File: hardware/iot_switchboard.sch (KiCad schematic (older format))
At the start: 15 parts, among them IC1 ATTINY84-M, P1 CONN_01X05, P2 CONN_01X05, T1 CONN_01X01

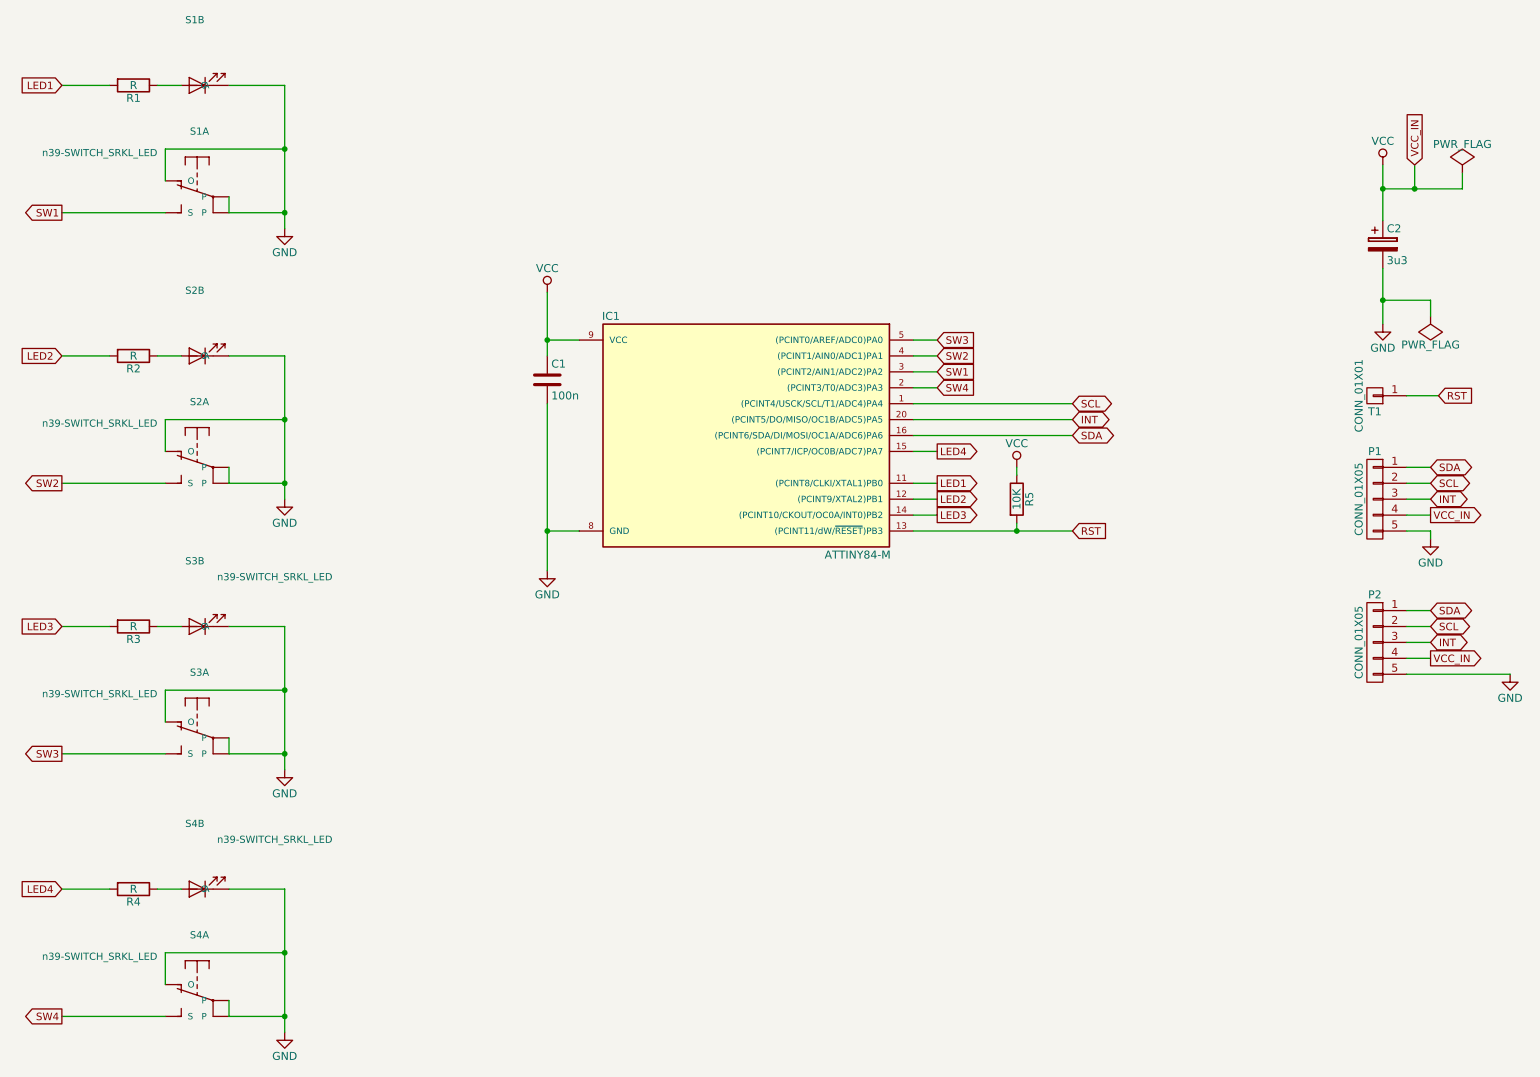
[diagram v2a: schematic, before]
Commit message: Reduce to 2 switches and adapt outline
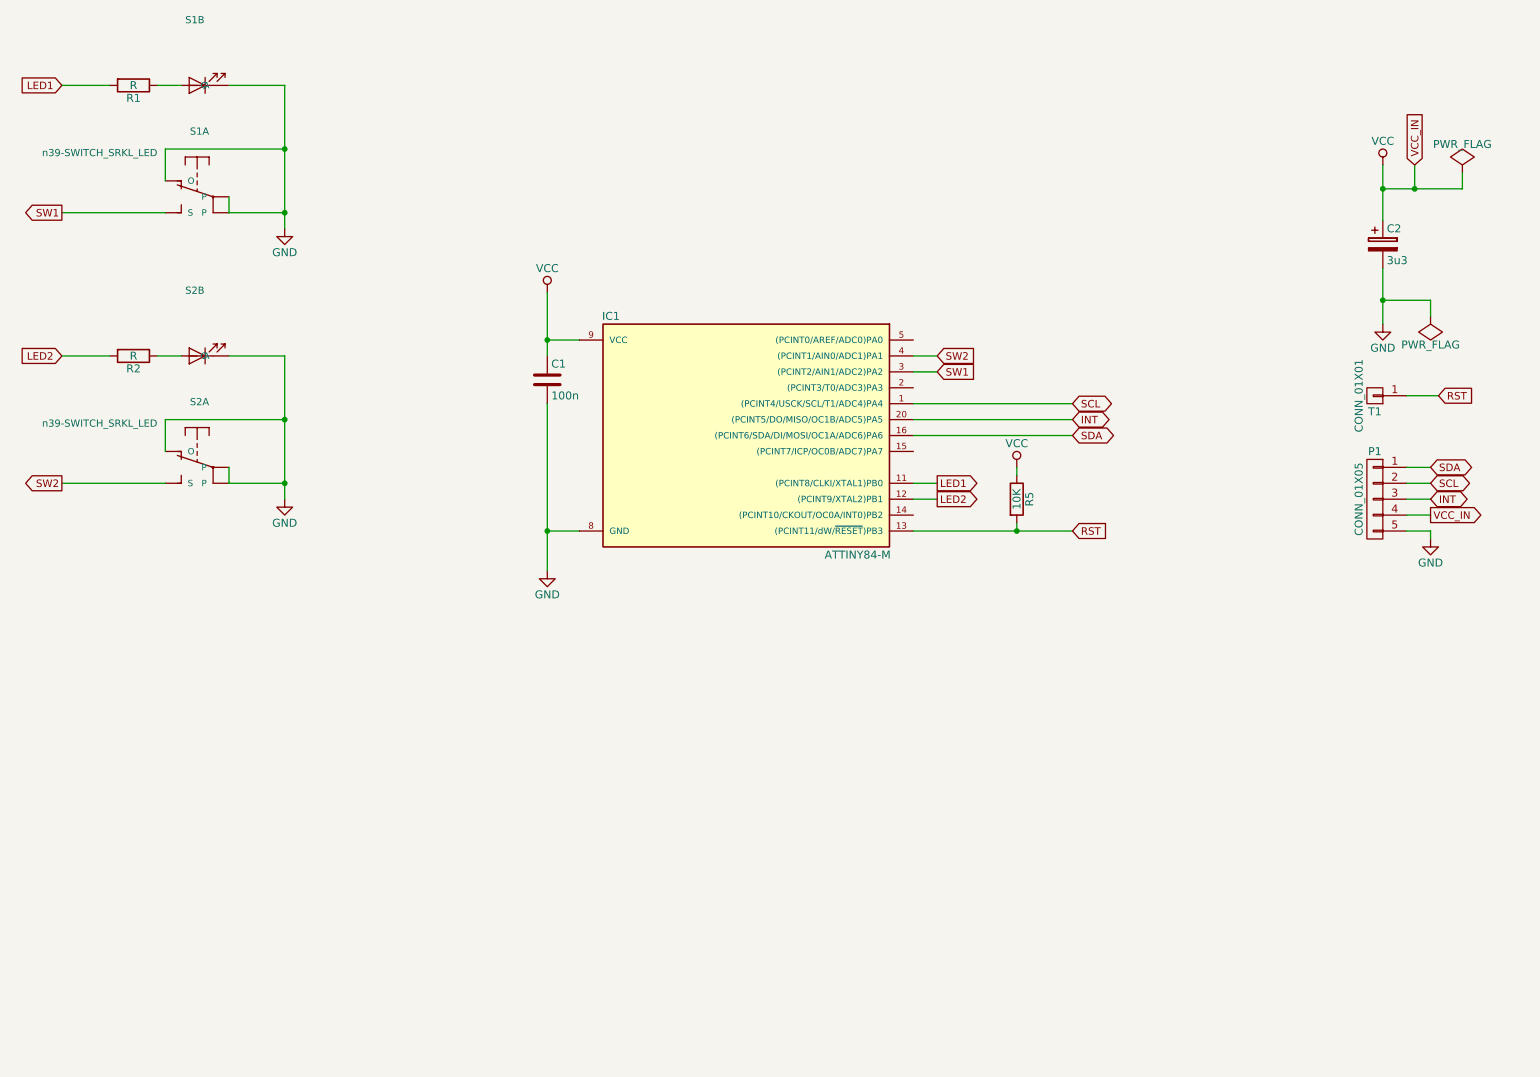
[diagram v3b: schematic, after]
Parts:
- removed P2: CONN_01X05, Socket_Strips:Socket_Strip_Straight_1x05, symbol CONN_01X05
- removed R3, R4: R, Resistors_Universal:Resistor_SMD+THTuniversal_0805to1206_RM10_HandSoldering, symbol R
- removed S3, S4: n39-SWITCH_SRKL_LED, n39-SWITCH_SRKL_LED, symbol n39-SWITCH_SRKL_LED
- P1: footprint Socket_Strips:Socket_Strip_Straight_1x05 -> Pin_Headers:Pin_Header_Straight_1x05
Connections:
- net LED3: no longer names the net of IC1.14 ((PCINT10/CKOUT/OC0A/INT0)PB2)
- net LED4: no longer names the net of IC1.15 ((PCINT7/ICP/OC0B/ADC7)PA7)
- net SW3: no longer names the net of IC1.5 ((PCINT0/AREF/ADC0)PA0)
- net SW4: no longer names the net of IC1.2 ((PCINT3/T0/ADC3)PA3)
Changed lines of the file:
@@
-$EndComp
-$Comp
-L n39-SWITCH_SRKL_LED S3
-U 1 1 58C873ED
-P 1900 5350
-F 0 "S3" V 1515 5275 45  0000 L BNN
-F 1 "n39-SWITCH_SRKL_LED" V 1650 5600 45  0000 L BNN
-F 2 "n39-SWITCH_SRKL_LED" H 1930 5500 20  0001 C CNN
-F 3 "" H 1900 5350 60  0001 C CNN
-	1    1900 5350
-	0    -1   1    0
-$EndComp
-$Comp
-L n39-SWITCH_SRKL_LED S3
-U 2 1 58C873F4
-P 1900 4650
-F 0 "S3" V 1515 4575 45  0000 L BNN
-F 1 "n39-SWITCH_SRKL_LED" V 1615 4775 45  0000 L BNN
-F 2 "n39-SWITCH_SRKL_LED" H 1930 4800 20  0001 C CNN
-F 3 "" H 1900 4650 60  0001 C CNN
-	2    1900 4650
-	0    1    1    0
-$EndComp
-$Comp
-L R R3
-U 1 1 58C873FB
-P 1500 4650
-F 0 "R3" V 1580 4650 50  0000 C CNN
-F 1 "R" V 1500 4650 50  0000 C CNN
-F 2 "Resistors_Universal:Resistor_SMD+THTuniversal_0805to1206_RM10_HandSoldering" V 1430 4650 50  0001 C CNN
-F 3 "" H 1500 4650 50  0000 C CNN
-	1    1500 4650
-	0    1    1    0
 $EndComp
 $Comp
 L GND #PWR03
-U 1 1 58C87402
-P 2450 5550
-F 0 "#PWR03" H 2450 5300 50  0001 C CNN
-F 1 "GND" H 2450 5400 50  0000 C CNN
-F 2 "" H 2450 5550 50  0000 C CNN
-F 3 "" H 2450 5550 50  0000 C CNN
-	1    2450 5550
-	1    0    0    -1
-$EndComp
-$Comp
-L n39-SWITCH_SRKL_LED S4
-U 1 1 58C87589
-P 1900 7000
-F 0 "S4" V 1515 6925 45  0000 L BNN
-F 1 "n39-SWITCH_SRKL_LED" V 1650 7250 45  0000 L BNN
-F 2 "n39-SWITCH_SRKL_LED" H 1930 7150 20  0001 C CNN
-F 3 "" H 1900 7000 60  0001 C CNN
-	1    1900 7000
-	0    -1   1    0
-$EndComp
-$Comp
-L n39-SWITCH_SRKL_LED S4
-U 2 1 58C87590
-P 1900 6300
-F 0 "S4" V 1515 6225 45  0000 L BNN
-F 1 "n39-SWITCH_SRKL_LED" V 1615 6425 45  0000 L BNN
-F 2 "n39-SWITCH_SRKL_LED" H 1930 6450 20  0001 C CNN
-F 3 "" H 1900 6300 60  0001 C CNN
-	2    1900 6300
-	0    1    1    0
-$EndComp
-$Comp
-L R R4
-U 1 1 58C87597
-P 1500 6300
-F 0 "R4" V 1580 6300 50  0000 C CNN
-F 1 "R" V 1500 6300 50  0000 C CNN
-F 2 "Resistors_Universal:Resistor_SMD+THTuniversal_0805to1206_RM10_HandSoldering" V 1430 6300 50  0001 C CNN
-F 3 "" H 1500 6300 50  0000 C CNN
-	1    1500 6300
-	0    1    1    0
-$EndComp
-$Comp
-L GND #PWR04
-U 1 1 58C8759E
-P 2450 7200
-F 0 "#PWR04" H 2450 6950 50  0001 C CNN
-F 1 "GND" H 2450 7050 50  0000 C CNN
-F 2 "" H 2450 7200 50  0000 C CNN
-F 3 "" H 2450 7200 50  0000 C CNN
-	1    2450 7200
-	1    0    0    -1
-$EndComp
-$Comp
-L GND #PWR05
 U 1 1 58C8805A
 P 4100 4300
-F 0 "#PWR05" H 4100 4050 50  0001 C CNN
+F 0 "#PWR03" H 4100 4050 50  0001 C CNN
 F 1 "GND" H 4100 4150 50  0000 C CNN
 F 2 "" H 4100 4300 50  0000 C CNN
@@
 $EndComp
 $Comp
-L VCC #PWR06
+L VCC #PWR04
 U 1 1 58C880BC
 P 4100 2550
-F 0 "#PWR06" H 4100 2400 50  0001 C CNN
+F 0 "#PWR04" H 4100 2400 50  0001 C CNN
 F 1 "VCC" H 4100 2700 50  0000 C CNN
 F 2 "" H 4100 2550 50  0000 C CNN
@@
 	1350 2950 1050 2950
 Wire Wire Line
-	2450 5450 2100 5450
-Wire Wire Line
-	2450 4650 2450 5550
-Wire Wire Line
-	2100 4650 2450 4650
-Connection ~ 2450 5450
-Wire Wire Line
-	1650 4650 1800 4650
-Wire Wire Line
-	1350 4650 1050 4650
-Wire Wire Line
-	2450 7100 2100 7100
-Wire Wire Line
-	2450 6300 2450 7200
-Wire Wire Line
-	2100 6300 2450 6300
-Connection ~ 2450 7100
-Wire Wire Line
-	1650 6300 1800 6300
-Wire Wire Line
-	1350 6300 1050 6300
-Wire Wire Line
 	4100 2550 4100 2950
 Wire Wire Line
@@
 $EndComp
 $Comp
-L VCC #PWR07
+L VCC #PWR05
 U 1 1 58C8935E
 P 7050 3650
-F 0 "#PWR07" H 7050 3500 50  0001 C CNN
+F 0 "#PWR05" H 7050 3500 50  0001 C CNN
 F 1 "VCC" H 7050 3800 50  0000 C CNN
 F 2 "" H 7050 3650 50  0000 C CNN
@@
 Text GLabel 1050 2950 0    47   Input ~ 0
 LED2
-Text GLabel 1050 4650 0    47   Input ~ 0
-LED3
-Text GLabel 1050 6300 0    47   Input ~ 0
-LED4
 Text GLabel 6550 3750 2    47   Output ~ 0
 LED1
 Text GLabel 6550 3850 2    47   Output ~ 0
 LED2
-Text GLabel 6550 3950 2    47   Output ~ 0
-LED3
-Text GLabel 6550 3550 2    47   Output ~ 0
-LED4
 Text GLabel 6550 3050 2    47   Input ~ 0
 SW1
 Text GLabel 6550 2950 2    47   Input ~ 0
 SW2
-Text GLabel 6550 2850 2    47   Input ~ 0
-SW3
-Text GLabel 6550 3150 2    47   Input ~ 0
-SW4
 Text GLabel 1050 2050 0    47   Output ~ 0
 SW1
 Text GLabel 1050 3750 0    47   Output ~ 0
 SW2
-Text GLabel 1050 5450 0    47   Output ~ 0
-SW3
-Text GLabel 1050 7100 0    47   Output ~ 0
-SW4
 Text GLabel 7400 4050 2    47   Input ~ 0
 RST
@@
 SDA
 $Comp
-L VCC #PWR08
+L VCC #PWR06
 U 1 1 58C8C38E
 P 9350 1750
-F 0 "#PWR08" H 9350 1600 50  0001 C CNN
+F 0 "#PWR06" H 9350 1600 50  0001 C CNN
 F 1 "VCC" H 9350 1900 50  0000 C CNN
 F 2 "" H 9350 1750 50  0000 C CNN
@@
 $EndComp
 $Comp
-L GND #PWR09
+L GND #PWR07
 U 1 1 58C8C3DE
 P 9350 2750
-F 0 "#PWR09" H 9350 2500 50  0001 C CNN
+F 0 "#PWR07" H 9350 2500 50  0001 C CNN
 F 1 "GND" H 9350 2600 50  0000 C CNN
 F 2 "" H 9350 2750 50  0000 C CNN
@@
 F 0 "P1" H 9300 4150 50  0000 C CNN
 F 1 "CONN_01X05" V 9400 3850 50  0000 C CNN
-F 2 "Socket_Strips:Socket_Strip_Straight_1x05" H 9300 3850 50  0001 C CNN
+F 2 "Pin_Headers:Pin_Header_Straight_1x05" H 9300 3850 50  0001 C CNN
 F 3 "" H 9300 3850 50  0000 C CNN
 	1    9300 3850
@@
 INT
 $Comp
-L GND #PWR010
+L GND #PWR08
 U 1 1 58C8F67F
 P 9650 4100
-F 0 "#PWR010" H 9650 3850 50  0001 C CNN
+F 0 "#PWR08" H 9650 3850 50  0001 C CNN
 F 1 "GND" H 9650 3950 50  0000 C CNN
 F 2 "" H 9650 4100 50  0000 C CNN
@@
 Connection ~ 9350 1900
 $Comp
-L PWR_FLAG #FLG011
+L PWR_FLAG #FLG09
 U 1 1 58C91D70
 P 9850 1800
-F 0 "#FLG011" H 9850 1895 50  0001 C CNN
+F 0 "#FLG09" H 9850 1895 50  0001 C CNN
 F 1 "PWR_FLAG" H 9850 1980 50  0000 C CNN
 F 2 "" H 9850 1800 50  0000 C CNN
@@
 Connection ~ 9550 1900
 $Comp
-L PWR_FLAG #FLG012
+L PWR_FLAG #FLG010
 U 1 1 58C921F8
 P 9650 2700
-F 0 "#FLG012" H 9650 2795 50  0001 C CNN
+F 0 "#FLG010" H 9650 2795 50  0001 C CNN
 F 1 "PWR_FLAG" H 9650 2880 50  0000 C CNN
 F 2 "" H 9650 2700 50  0000 C CNN
@@
 $EndComp
 Wire Wire Line
-	6400 3550 6550 3550
-Wire Wire Line
-	6400 3950 6550 3950
-Wire Wire Line
 	2100 3650 2100 3750
 Wire Wire Line
@@
 	1700 3750 1050 3750
 Wire Wire Line
-	2100 5450 2100 5350
-Wire Wire Line
 	2100 1950 2100 2050
 Wire Wire Line
@@
 Wire Wire Line
 	1700 2050 1050 2050
-Wire Wire Line
-	1700 5450 1050 5450
-Wire Wire Line
-	2100 7100 2100 7000
-Wire Wire Line
-	1700 7100 1050 7100
 $Comp
 L ATTINY84-M IC1
@@
 $EndComp
 Wire Wire Line
-	9500 4550 9650 4550
-Wire Wire Line
-	9500 4650 9650 4650
-Wire Wire Line
-	9500 4750 9650 4750
-Wire Wire Line
-	9500 4950 10150 4950
-Text GLabel 9650 4550 2    47   BiDi ~ 0
-SDA
-Text GLabel 9650 4650 2    47   BiDi ~ 0
-SCL
-Text GLabel 9650 4750 2    47   BiDi ~ 0
-INT
-$Comp
-L GND #PWR013
-U 1 1 58CAFD4E
-P 10150 4950
-F 0 "#PWR013" H 10150 4700 50  0001 C CNN
-F 1 "GND" H 10150 4800 50  0000 C CNN
-F 2 "" H 10150 4950 50  0000 C CNN
-F 3 "" H 10150 4950 50  0000 C CNN
-	1    10150 4950
-	1    0    0    -1
-$EndComp
-Wire Wire Line
-	9500 4850 9650 4850
-Text GLabel 9650 4850 2    47   Output ~ 0
-VCC_IN
-Wire Wire Line
-	6400 2850 6550 2850
-Wire Wire Line
 	6550 2950 6400 2950
 Wire Wire Line
 	6550 3050 6400 3050
-Wire Wire Line
-	6550 3150 6400 3150
 Wire Wire Line
 	6400 3750 6550 3750
@@
 	1700 3350 2450 3350
 Connection ~ 2450 3350
-Wire Wire Line
-	1700 5250 1700 5050
-Wire Wire Line
-	1700 5050 2450 5050
-Connection ~ 2450 5050
-Wire Wire Line
-	1700 6900 1700 6700
-Wire Wire Line
-	1700 6700 2450 6700
-Connection ~ 2450 6700
 $Comp
 L CONN_01X01 T1
@@
 Wire Wire Line
 	9500 3200 9700 3200
-$Comp
-L CONN_01X05 P2
-U 1 1 58CDE56F
-P 9300 4750
-F 0 "P2" H 9300 5050 50  0000 C CNN
-F 1 "CONN_01X05" V 9400 4750 50  0000 C CNN
-F 2 "Socket_Strips:Socket_Strip_Straight_1x05" H 9300 4750 50  0001 C CNN
-F 3 "" H 9300 4750 50  0000 C CNN
-	1    9300 4750
-	-1   0    0    -1
-$EndComp
 $EndSCHEMATC

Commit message: New Layout
Yeah!
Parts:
- added R4, R5, R6: 0, Resistors_SMD:R_0402, symbol R
- renumbered R5 to R3
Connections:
- net GND: now also R4.1, R5.1, R6.1
- net SCL: now also P1.1 (P1); no longer P1.2 (P2)
- net SDA: now also P1.2 (P2); no longer P1.1 (P1)
- net SW1: now also IC1.5 ((PCINT0/AREF/ADC0)PA0); no longer IC1.3 ((PCINT2/AIN1/ADC2)PA2)
- net SW2: now also IC1.15 ((PCINT7/ICP/OC0B/ADC7)PA7); no longer IC1.4 ((PCINT1/AIN0/ADC1)PA1)
- net at IC1.2 ((PCINT3/T0/ADC3)PA3): now also R4.2
- new net: IC1.3 ((PCINT2/AIN1/ADC2)PA2), R5.2
- new net: IC1.4 ((PCINT1/AIN0/ADC1)PA1), R6.2
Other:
- note added: "I2C Address"
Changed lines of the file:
@@
 Connection ~ 4100 4050
 Wire Wire Line
-	6400 3350 7400 3350
-Wire Wire Line
-	6400 3250 7400 3250
-Wire Wire Line
 	6400 4050 7400 4050
 $Comp
-L R R5
+L R R3
 U 1 1 58C89309
 P 7050 3850
-F 0 "R5" V 7130 3850 50  0000 C CNN
+F 0 "R3" V 7130 3850 50  0000 C CNN
 F 1 "10K" V 7050 3850 50  0000 C CNN
 F 2 "Resistors_SMD:R_0603_HandSoldering" V 6980 3850 50  0001 C CNN
@@
 Text GLabel 6550 3850 2    47   Output ~ 0
 LED2
-Text GLabel 6550 3050 2    47   Input ~ 0
+Text GLabel 6550 2850 2    47   Input ~ 0
 SW1
-Text GLabel 6550 2950 2    47   Input ~ 0
+Text GLabel 6550 3550 2    47   Input ~ 0
 SW2
 Text GLabel 1050 2050 0    47   Output ~ 0
@@
 Text GLabel 7400 4050 2    47   Input ~ 0
 RST
-Text GLabel 7400 3250 2    47   BiDi ~ 0
+Text GLabel 6550 3250 2    47   BiDi ~ 0
 SCL
-Text GLabel 7400 3350 2    47   BiDi ~ 0
+Text GLabel 6550 3350 2    47   BiDi ~ 0
 INT
-Text GLabel 7400 3450 2    47   BiDi ~ 0
+Text GLabel 6550 3450 2    47   BiDi ~ 0
 SDA
 $Comp
@@
 $EndComp
 Wire Wire Line
-	9500 3650 9650 3650
-Wire Wire Line
-	9500 3750 9650 3750
-Wire Wire Line
 	9500 3850 9650 3850
 Wire Wire Line
 	9500 4050 9650 4050
+Text GLabel 9650 3750 2    47   BiDi ~ 0
+SDA
 Text GLabel 9650 3650 2    47   BiDi ~ 0
-SDA
-Text GLabel 9650 3750 2    47   BiDi ~ 0
 SCL
 Text GLabel 9650 3850 2    47   BiDi ~ 0
@@
 $EndComp
 Wire Wire Line
-	6550 2950 6400 2950
-Wire Wire Line
-	6550 3050 6400 3050
-Wire Wire Line
 	6400 3750 6550 3750
 Wire Wire Line
@@
 Text GLabel 9700 3200 2    47   Input ~ 0
 RST
-Wire Wire Line
-	6400 3450 7400 3450
 Wire Wire Line
 	1700 1850 1700 1650
@@
 Wire Wire Line
 	9500 3200 9700 3200
+Wire Wire Line
+	6400 2850 6550 2850
+Wire Wire Line
+	6400 3550 6550 3550
+Wire Wire Line
+	9500 3650 9650 3650
+Wire Wire Line
+	9500 3750 9650 3750
+$Comp
+L R R6
+U 1 1 58F21A9A
+P 6650 2950
+F 0 "R6" V 6600 3150 50  0000 C CNN
+F 1 "0" V 6650 2950 50  0000 C CNN
+F 2 "Resistors_SMD:R_0402" V 6580 2950 50  0001 C CNN
+F 3 "" H 6650 2950 50  0000 C CNN
+	1    6650 2950
+	0    1    1    0
+$EndComp
+$Comp
+L R R5
+U 1 1 58F21B1B
+P 6650 3050
+F 0 "R5" V 6600 3250 50  0000 C CNN
+F 1 "0" V 6650 3050 50  0000 C CNN
+F 2 "Resistors_SMD:R_0402" V 6580 3050 50  0001 C CNN
+F 3 "" H 6650 3050 50  0000 C CNN
+	1    6650 3050
+	0    1    1    0
+$EndComp
+$Comp
+L R R4
+U 1 1 58F21B68
+P 6650 3150
+F 0 "R4" V 6600 3350 50  0000 C CNN
+F 1 "0" V 6650 3150 50  0000 C CNN
+F 2 "Resistors_SMD:R_0402" V 6580 3150 50  0001 C CNN
+F 3 "" H 6650 3150 50  0000 C CNN
+	1    6650 3150
+	0    1    1    0
+$EndComp
+$Comp
+L GND #PWR011
+U 1 1 58F21E46
+P 7050 3200
+F 0 "#PWR011" H 7050 2950 50  0001 C CNN
+F 1 "GND" H 7050 3050 50  0000 C CNN
+F 2 "" H 7050 3200 50  0000 C CNN
+F 3 "" H 7050 3200 50  0000 C CNN
+	1    7050 3200
+	1    0    0    -1
+$EndComp
+Wire Wire Line
+	6800 3150 7050 3150
+Wire Wire Line
+	6800 3050 7050 3050
+Connection ~ 7050 3050
+Wire Wire Line
+	6800 2950 7050 2950
+Connection ~ 7050 2950
+Wire Wire Line
+	6400 2950 6500 2950
+Wire Wire Line
+	6400 3050 6500 3050
+Wire Wire Line
+	6400 3150 6500 3150
+Text Notes 6950 2900 0    60   ~ 0
+I2C Address
+Wire Wire Line
+	6400 3250 6550 3250
+Wire Wire Line
+	6400 3350 6550 3350
+Wire Wire Line
+	6400 3450 6550 3450
+Wire Wire Line
+	7050 2950 7050 3200
+Connection ~ 7050 3150
 $EndSCHEMATC
